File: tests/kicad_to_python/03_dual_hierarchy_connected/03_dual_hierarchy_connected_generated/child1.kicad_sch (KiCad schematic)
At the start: 1 part

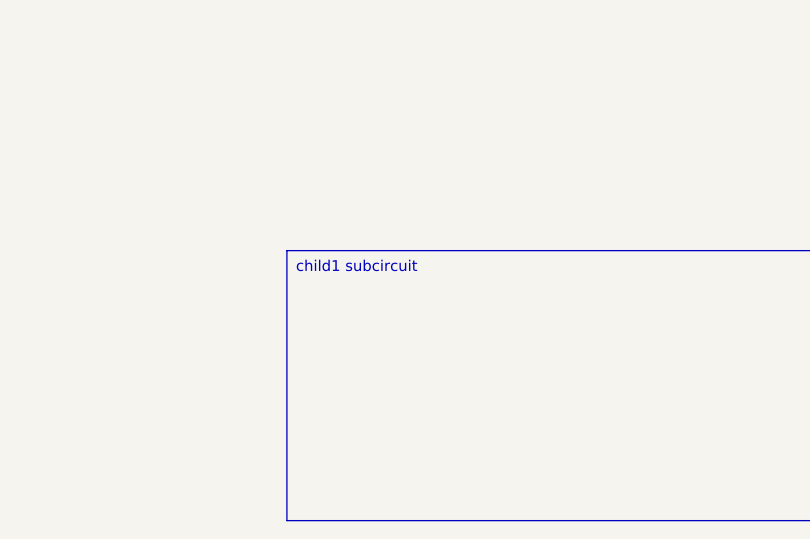
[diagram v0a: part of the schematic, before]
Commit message: Add comprehensive edge case testing for multi-file KiCad to Python conversion
- **Comprehensive edge case coverage**: Tests single circuits, hierarchical designs,
  empty circuits, invalid net names, partially shared nets, and multi-level hierarchy
- **Production-ready unit tests**: 12 test cases in test_python_code_generator_edge_cases.py
  covering all major scenarios with proper pytest fixtures and temporary directories
- **Integration test script**: test_edge_cases.py provides comprehensive testing against
  real KiCad projects and programmatic edge cases with detailed logging
- **Robust multi-file generation**: Enhanced PythonCodeGenerator with separate file
  generation, proper net parameter passing, and shared net detection
- **Net sanitization improvements**: Handles complex net names (+3.3V, signal/with/slashes)
  with proper Python variable name conversion
- **Hierarchical design support**: Automatic detection of hierarchical vs flat designs
  with appropriate code generation strategies
- **Regression prevention**: All edge cases now have automated tests to prevent future
  regressions in the multi-file architecture

The multi-file KiCad to Python conversion functionality is now comprehensively tested
and production-ready, supporting real-world hierarchical circuit designs with proper
net connectivity and parameter passing.

🤖 Generated with [Claude Code](https://claude.ai/code)

Co-Authored-By: Claude <noreply@anthropic.com>
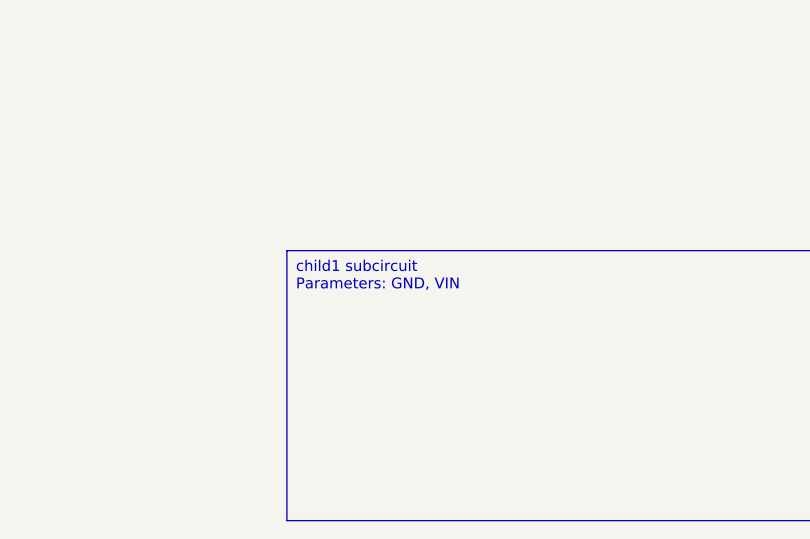
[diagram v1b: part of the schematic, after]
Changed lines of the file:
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@@
 				"03_dual_hierarchy_connected_generated"
 				(path
-					"/1a01bfd2-50a0-43d4-a3b2-c177f30ae91a/df37d547-ba63-4a31-b192-4a9c30f04664/bba911a4-8e43-4c7c-a570-6af66e3e142d"
+					"/8d6015ca-7df9-48d5-b783-169efd3b2bf3/ab203ed3-134f-47e9-880d-37f628e82570/744d19a2-f42a-41fb-99ae-32071e58c473"
 					(reference R2)
 					(unit 1)
@@
 	)
 	(text_box
-		"child1 subcircuit"
+		"child1 subcircuit\n    Parameters: GND, VIN"
 		(exclude_from_sim yes)
 		(at 184.0 110.0 0)
@@
 	(sheet_instances
 		(path
-			"/1a01bfd2-50a0-43d4-a3b2-c177f30ae91a/df37d547-ba63-4a31-b192-4a9c30f04664/bba911a4-8e43-4c7c-a570-6af66e3e142d"
+			"/8d6015ca-7df9-48d5-b783-169efd3b2bf3/ab203ed3-134f-47e9-880d-37f628e82570/744d19a2-f42a-41fb-99ae-32071e58c473"
 			(page "1")
 		)
